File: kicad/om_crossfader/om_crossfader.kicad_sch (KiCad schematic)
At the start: 23 parts, among them J1 Conn_01x09_Pin, U3 NE5532, U4 NE5532, U5 NE5532, U6 NE5532

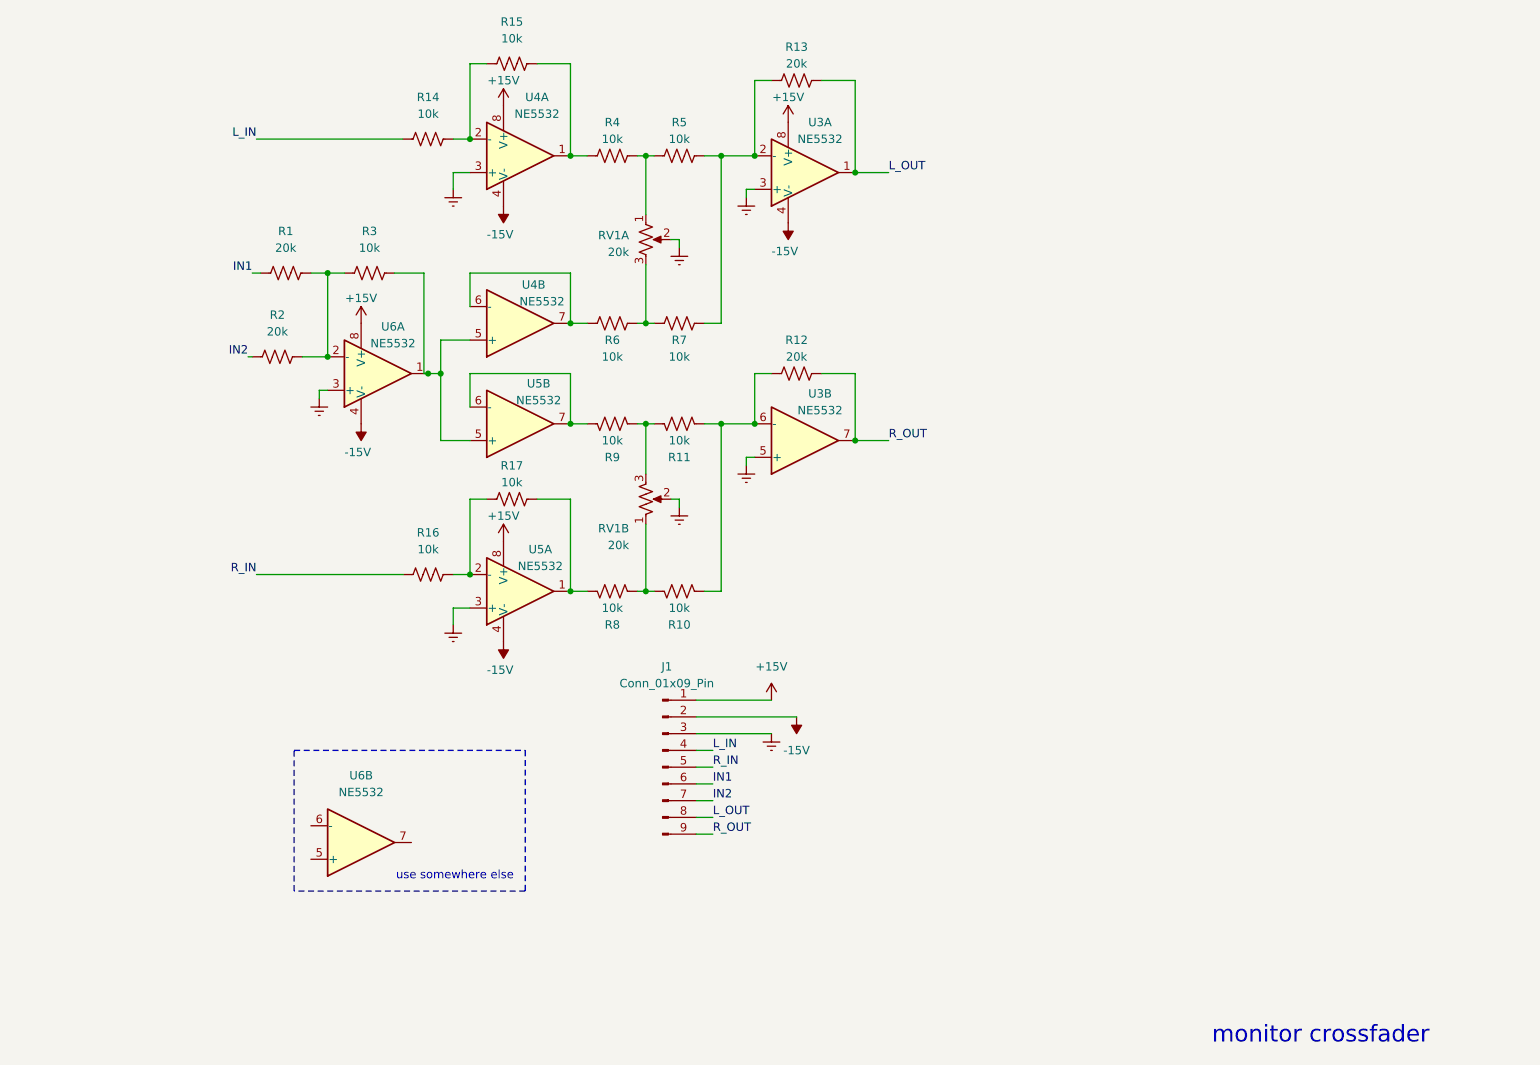
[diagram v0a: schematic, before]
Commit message: direct monitor switch (#5)
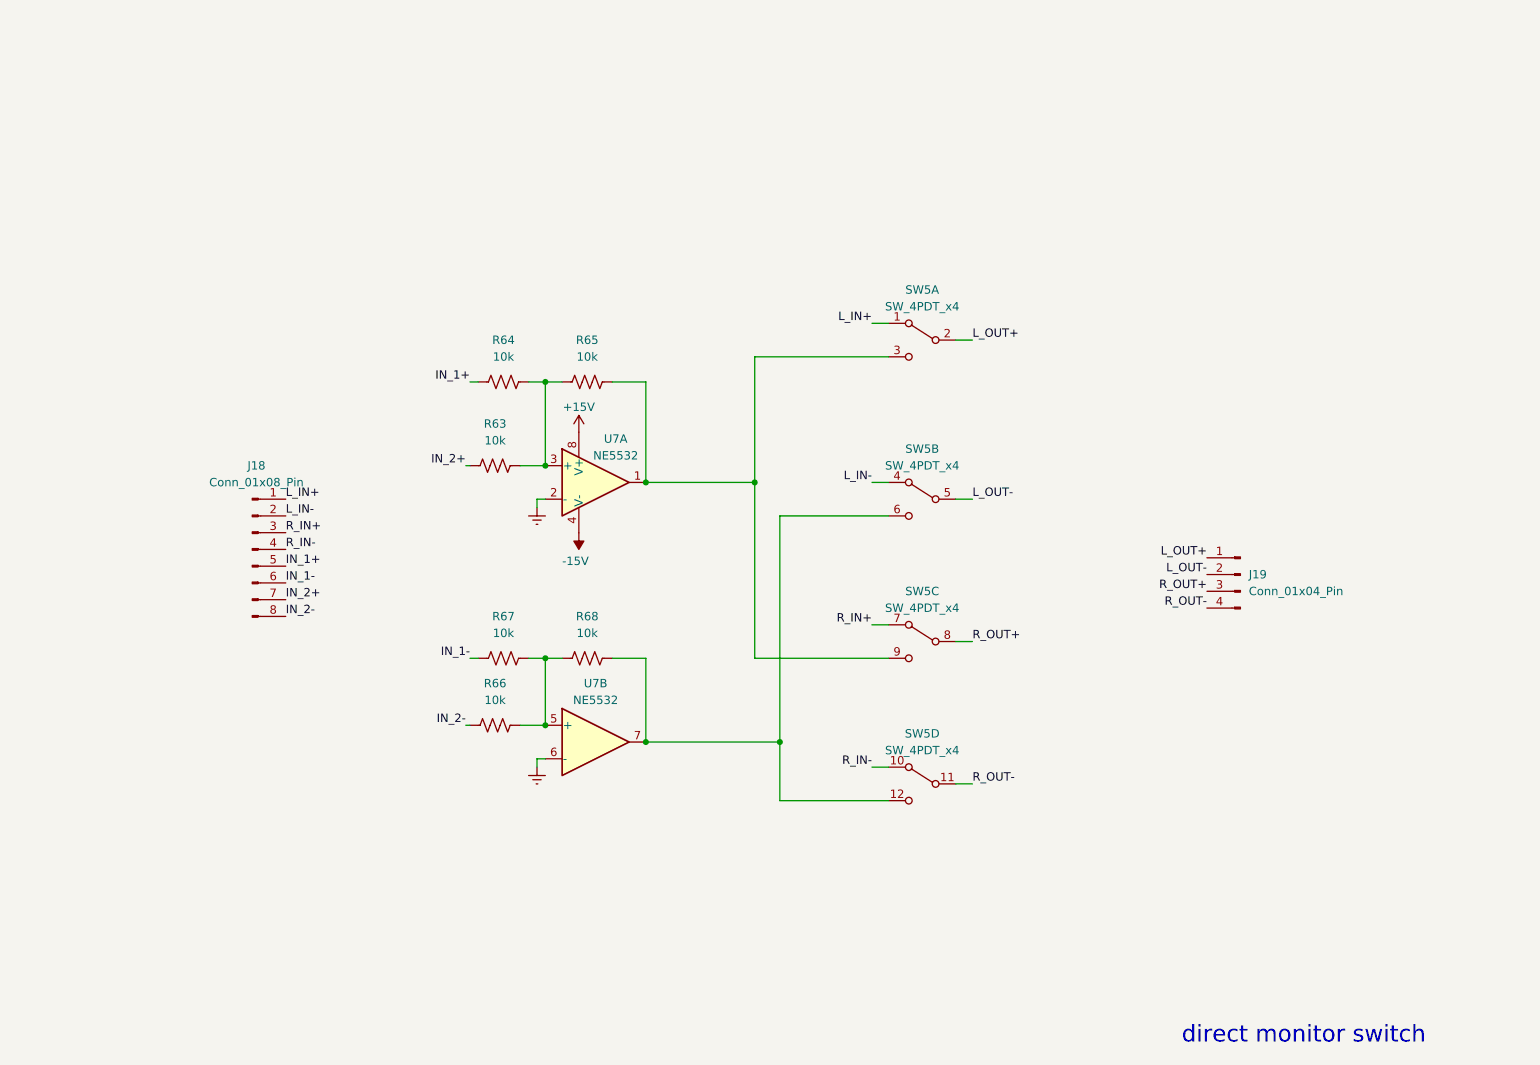
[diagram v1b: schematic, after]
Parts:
- removed J1: Conn_01x09_Pin, symbol Connector:Conn_01x09_Pin
- removed R1, R12, R13, R2: 20k, symbol Device:R_US
- removed R10, R11, R14, R15, R16, R17, R3, R4, R5, R6, R7, R8, R9: 10k, symbol Device:R_US
- removed RV1: 20k, symbol openmic:R_Potentiometer_US_Dual
- removed U3, U4, U5, U6: NE5532, symbol Amplifier_Operational:NE5532
- added J18: Conn_01x08_Pin, symbol Connector:Conn_01x08_Pin
- added J19: Conn_01x04_Pin, symbol Connector:Conn_01x04_Pin
- added R63, R64, R65, R66, R67, R68: 10k, symbol Device:R_US
- added SW5: SW_4PDT_x4, symbol openmic:SW_4PDT_x4
- added U7: NE5532, symbol Amplifier_Operational:NE5532
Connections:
- net +15V: now also U7.8 (V+)
- net -15V: now also U7.4 (V-)
- net Earth: now also U7.2 (-), U7.6 (-)
- new net: R63.2, R64.2, R65.1, U7.3 (+)
- new net: R66.2, R67.2, R68.1, U7.5 (+)
- new net: R65.2, SW5.3 (C), SW5.9 (C), U7.1
- new net: R68.2, SW5.12 (C), SW5.6 (C), U7.7
- new net IN_1+: J18.5 (Pin_5), R64.1
- new net IN_1-: J18.6 (Pin_6), R67.1
- new net IN_2+: J18.7 (Pin_7), R63.1
- new net IN_2-: J18.8 (Pin_8), R66.1
- new net L_IN+: J18.1 (Pin_1), SW5.1 (A)
- new net L_IN-: J18.2 (Pin_2), SW5.4 (A)
- new net L_OUT+: J19.1 (Pin_1), SW5.2 (B)
- new net L_OUT-: J19.2 (Pin_2), SW5.5 (B)
- new net R_IN+: J18.3 (Pin_3), SW5.7 (A)
- new net R_IN-: J18.4 (Pin_4), SW5.10 (A)
- new net R_OUT+: J19.3 (Pin_3), SW5.8 (B)
- new net R_OUT-: J19.4 (Pin_4), SW5.11 (B)
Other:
- note added: "direct monitor switch"
- note removed: "monitor crossfader"
- note removed: "use somewhere else"

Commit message: line output gain staging
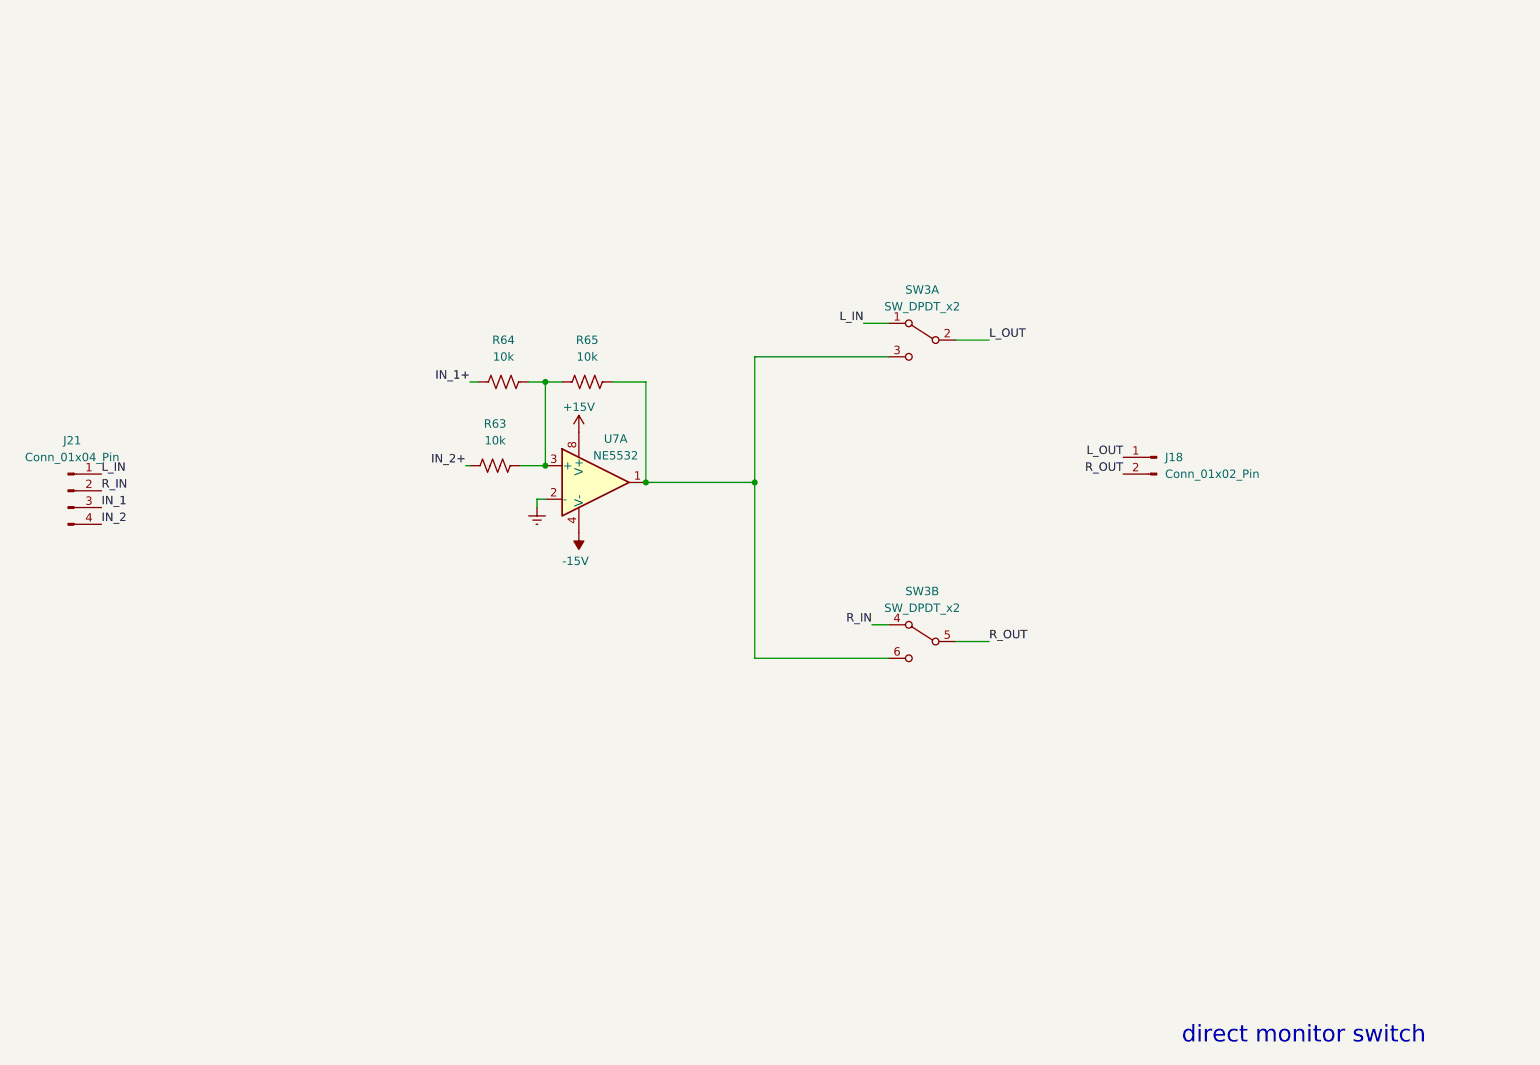
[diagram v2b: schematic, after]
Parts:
- removed J18: Conn_01x08_Pin, symbol Connector:Conn_01x08_Pin
- removed J19: Conn_01x04_Pin, symbol Connector:Conn_01x04_Pin
- removed R66, R67, R68: 10k, symbol Device:R_US
- removed SW5: SW_4PDT_x4, symbol openmic:SW_4PDT_x4
- removed unit 2 of U7
- added J18: Conn_01x02_Pin, symbol Connector:Conn_01x02_Pin
- added J21: Conn_01x04_Pin, symbol Connector:Conn_01x04_Pin
- added SW3: SW_DPDT_x2, symbol openmic:SW_DPDT_x2
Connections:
- net at R65.2, U7.1: now also SW3.3 (C), SW3.6 (C)
- new net IN_1: J21.3 (Pin_3)
- new net IN_2: J21.4 (Pin_4)
- new net L_IN: J21.1 (Pin_1), SW3.1 (A)
- new net L_OUT: J18.1 (Pin_1), SW3.2 (B)
- new net R_IN: J21.2 (Pin_2), SW3.4 (A)
- new net R_OUT: J18.2 (Pin_2), SW3.5 (B)
